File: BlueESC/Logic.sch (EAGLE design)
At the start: 33 parts, among them U1 ATMEGA168, U2 V_REG_LDOSMD, Y1 RESONATORSMD

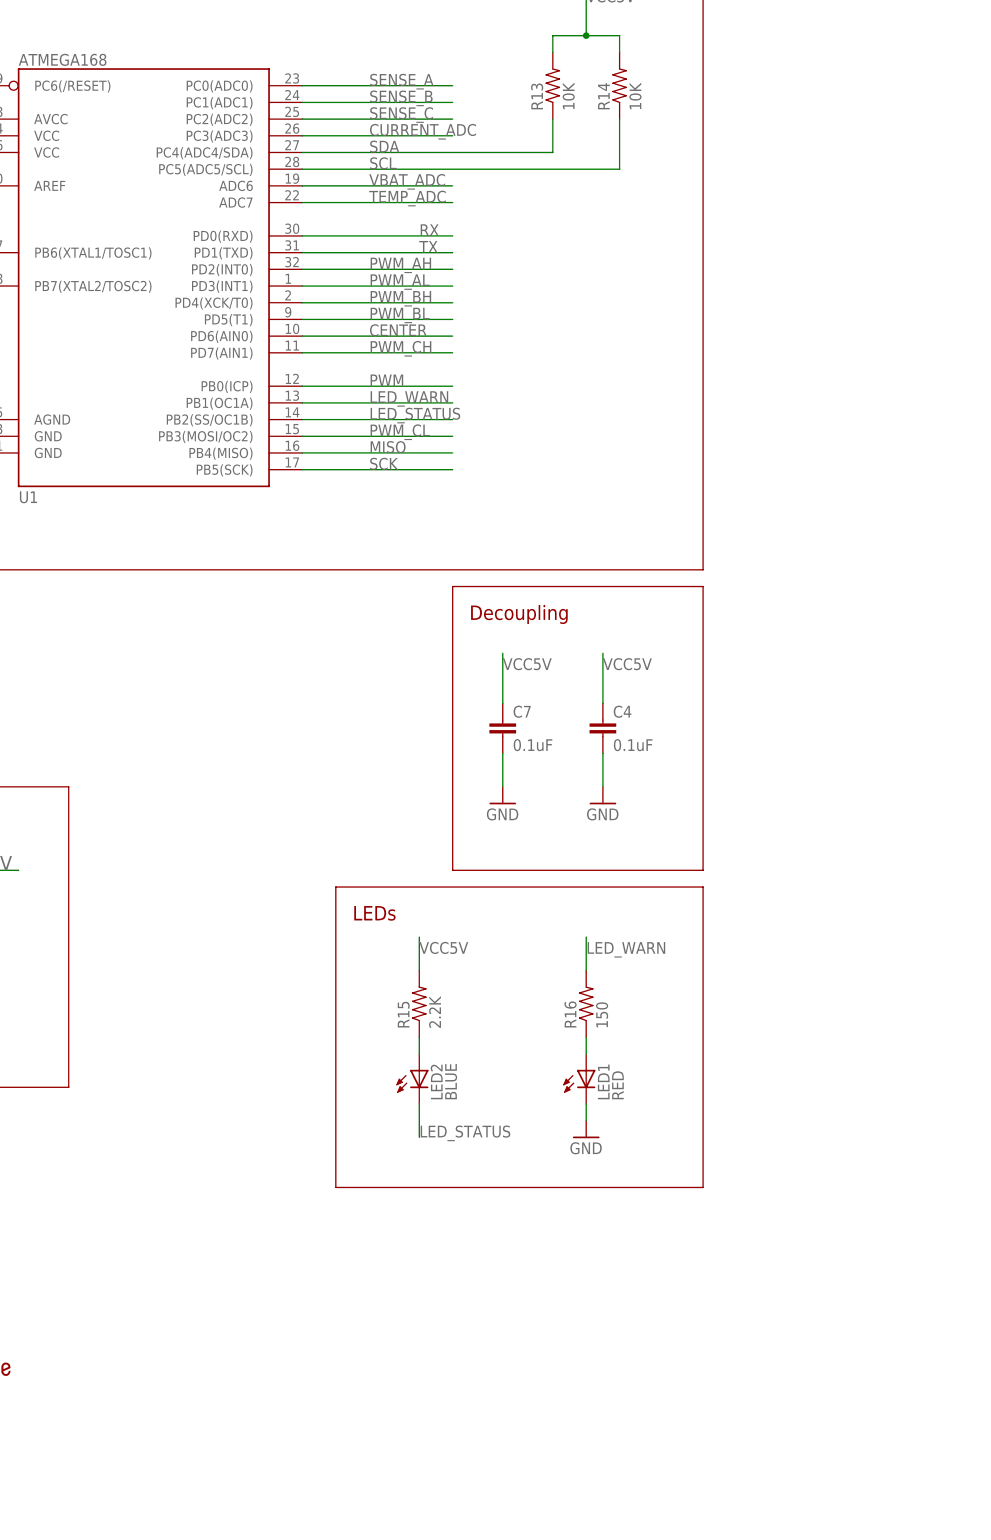
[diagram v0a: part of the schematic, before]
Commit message: Switch to SMT LEDs.
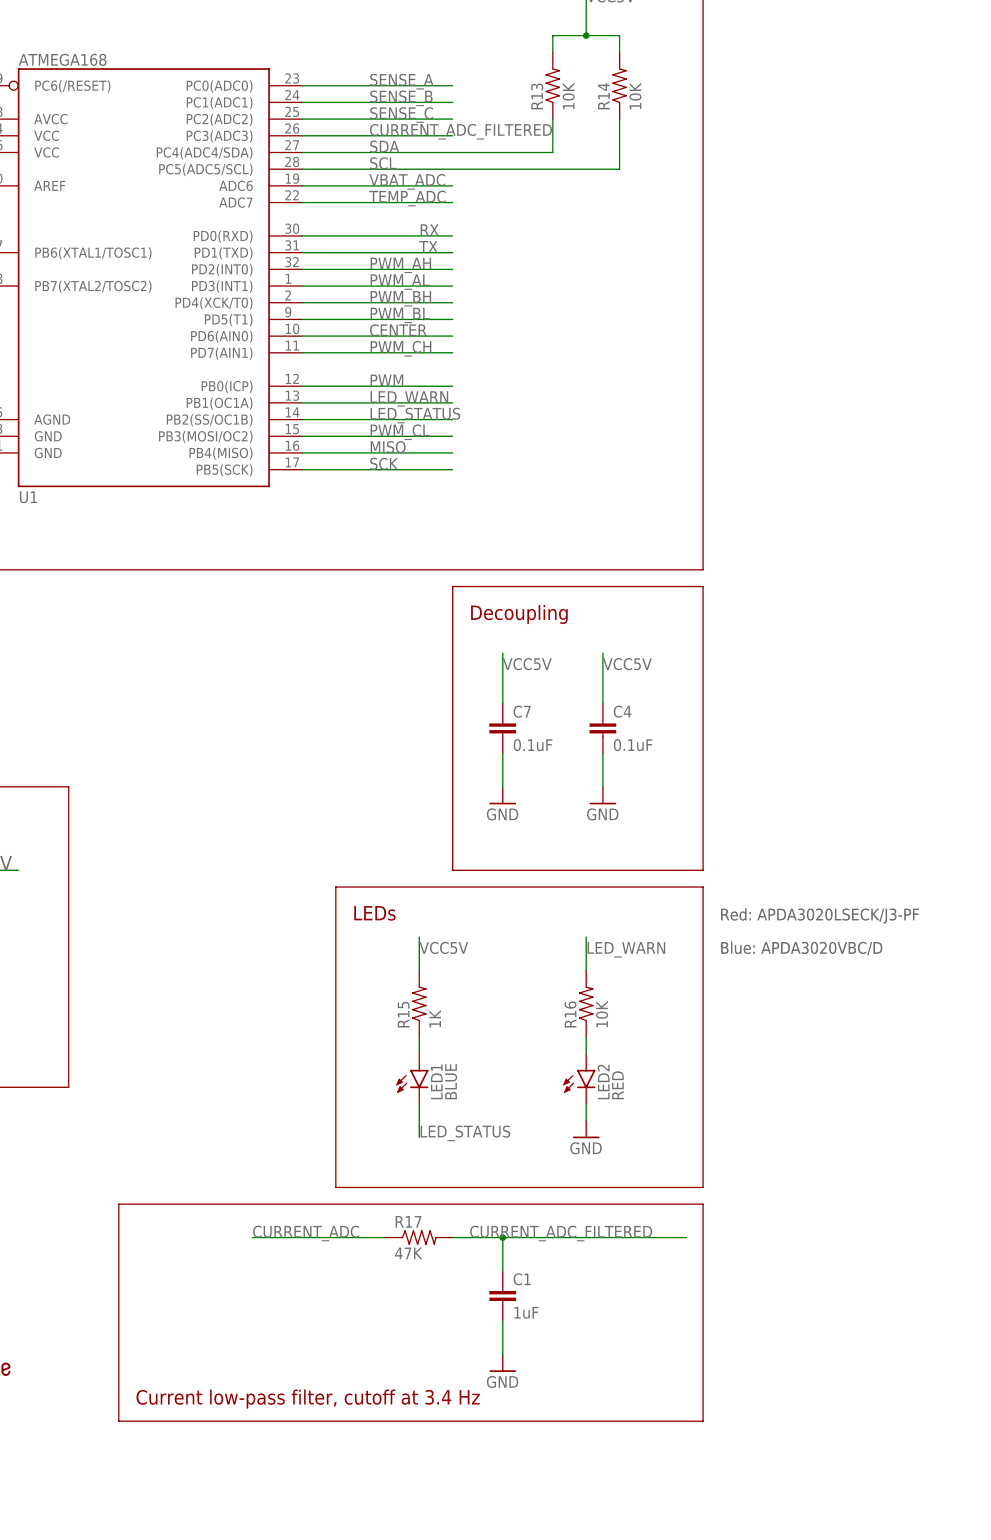
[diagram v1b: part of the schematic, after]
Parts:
- added C1: 1uF, SparkFun-Capacitors:CAP0603-CAP
- added R17: 47K, SparkFun:RESISTOR0603-RES
- LED1: value RED -> BLUE; device SparkFun:LED3MM -> BR-Eagle-Library:LED3X2-RA
- LED2: value BLUE -> RED; device SparkFun:LED3MM -> BR-Eagle-Library:LED3X2-RA
- R15: value 2.2K -> 1K
- R16: value 150 -> 10K
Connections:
- new net CURRENT_ADC_FILTERED: C1.1, R17.2, U1.PC3(ADC3)
- net CURRENT_ADC: now also R17.1; no longer U1.PC3(ADC3)
- net GND: now also C1.2, LED2.C; no longer LED1.C
- net LED_STATUS: now also LED1.C; no longer LED2.C
- net N$16: now also LED1.A; no longer LED2.A
- net N$3: now also LED2.A; no longer LED1.A
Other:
- note added: "Blue: APDA3020VBC/D"
- note added: "Current low-pass filter, cutoff at 3.4 Hz"
- note added: "Red: APDA3020LSECK/J3-PF"

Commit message: Added PWM pull-down resistor.
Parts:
- added R18: 10K, SparkFun:RESISTOR0603-RES
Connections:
- net GND: now also R18.1
- net PWM: now also R18.2
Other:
- note added: "PWM Pull-Down"
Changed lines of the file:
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@@
 <part name="LED1" library="BR-Eagle-Library" deviceset="LED" device="3X2-RA" value="BLUE"/>
 <part name="LED2" library="BR-Eagle-Library" deviceset="LED" device="3X2-RA" value="RED"/>
+<part name="R18" library="SparkFun" deviceset="RESISTOR" device="0603-RES" value="10K"/>
+<part name="GND6" library="SparkFun" deviceset="GND" device=""/>
 </parts>
 <sheets>
@@
 <text x="208.28" y="35.56" size="1.778" layer="97">Red: APDA3020LSECK/J3-PF</text>
 <text x="208.28" y="30.48" size="1.778" layer="97">Blue: APDA3020VBC/D</text>
+<text x="119.38" y="81.28" size="2.1844" layer="94" ratio="13">PWM Pull-Down</text>
 </plain>
 <instances>
@@
 <instance part="LED1" gate="G$1" x="162.56" y="12.7"/>
 <instance part="LED2" gate="G$1" x="187.96" y="12.7"/>
+<instance part="R18" gate="G$1" x="147.32" y="68.58" rot="R90"/>
+<instance part="GND6" gate="1" x="147.32" y="53.34"/>
 </instances>
 <busses>
@@
 <pinref part="C1" gate="G$1" pin="2"/>
 <wire x1="175.26" y1="-30.48" x2="175.26" y2="-25.4" width="0.1524" layer="91"/>
+</segment>
+<segment>
+<pinref part="GND6" gate="1" pin="GND"/>
+<pinref part="R18" gate="G$1" pin="1"/>
+<wire x1="147.32" y1="55.88" x2="147.32" y2="63.5" width="0.1524" layer="91"/>
 </segment>
 </net>
@@
 <label x="-5.08" y="-10.16" size="1.778" layer="95"/>
 </segment>
-</net>
+<segment>
+<pinref part="R18" gate="G$1" pin="2"/>
+<wire x1="147.32" y1="73.66" x2="147.32" y2="83.82" width="0.1524" layer="91"/>
+<label x="147.32" y="81.28" size="1.778" layer="95"/>
+</segment>
+</net>

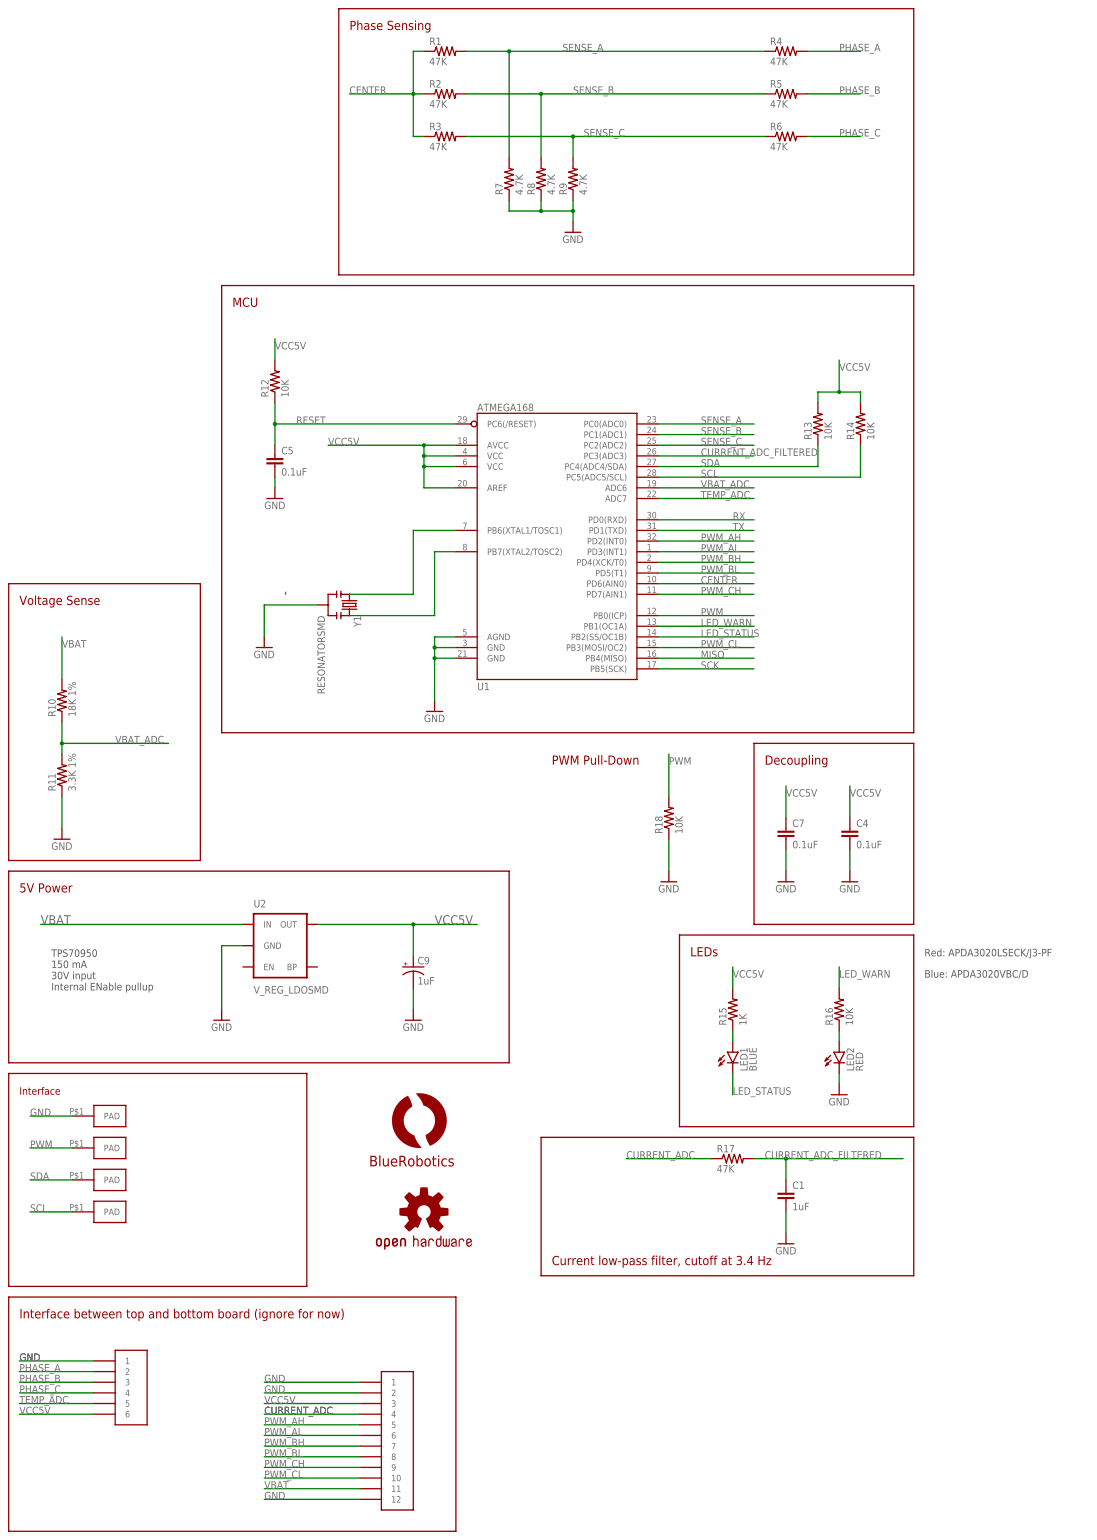
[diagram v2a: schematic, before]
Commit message: New logic board prototype ordered 8/14/15.
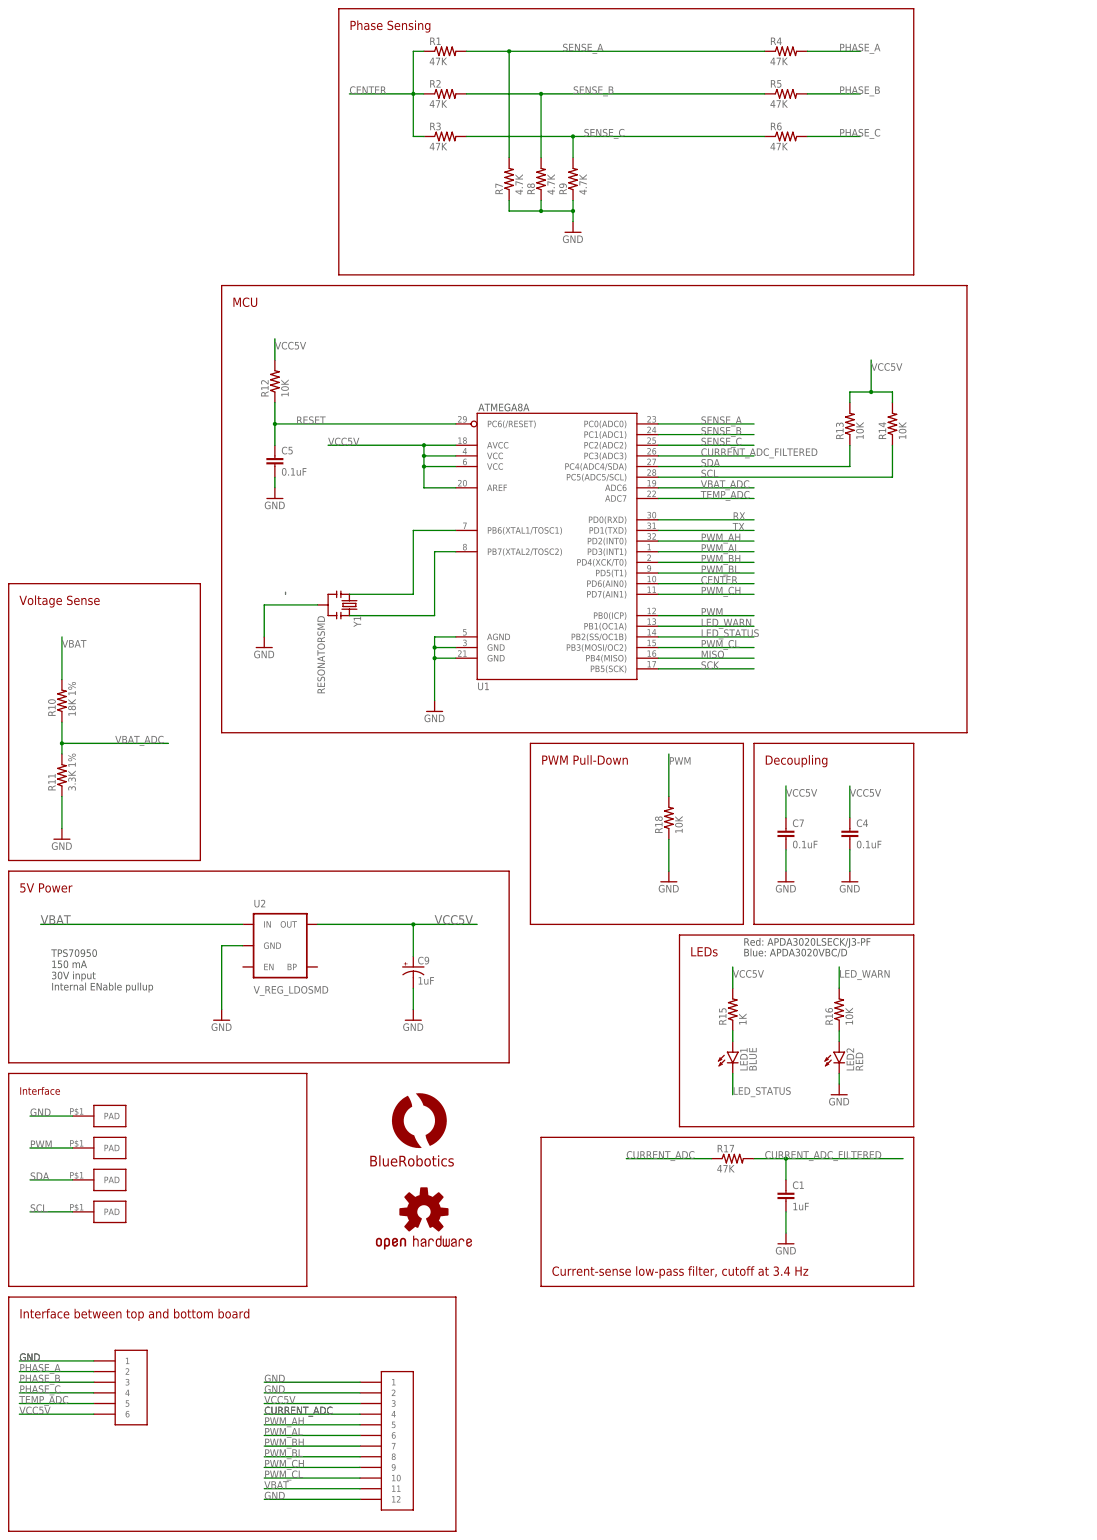
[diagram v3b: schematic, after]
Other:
- note added: "ATMEGA8A"
- note added: "Current-sense low-pass filter, cutoff at 3.4 Hz"
- note added: "Interface between top and bottom board"
- note removed: "Current low-pass filter, cutoff at 3.4 Hz"
- note removed: "Interface between top and bottom board (ignore for now)"
- moved on the sheet: R13, R14
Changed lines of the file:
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@@
 <plain>
 <wire x1="55.88" y1="122.428" x2="55.88" y2="121.92" width="0.2032" layer="97"/>
-<wire x1="40.64" y1="195.58" x2="205.74" y2="195.58" width="0.1524" layer="94"/>
-<wire x1="205.74" y1="195.58" x2="205.74" y2="88.9" width="0.1524" layer="94"/>
-<wire x1="205.74" y1="88.9" x2="40.64" y2="88.9" width="0.1524" layer="94"/>
+<wire x1="40.64" y1="195.58" x2="218.44" y2="195.58" width="0.1524" layer="94"/>
+<wire x1="218.44" y1="195.58" x2="218.44" y2="88.9" width="0.1524" layer="94"/>
+<wire x1="218.44" y1="88.9" x2="40.64" y2="88.9" width="0.1524" layer="94"/>
 <wire x1="40.64" y1="88.9" x2="40.64" y2="195.58" width="0.1524" layer="94"/>
 <text x="43.18" y="190.5" size="2.1844" layer="94" ratio="13">MCU</text>
@@
 <wire x1="96.52" y1="-101.6" x2="-10.16" y2="-101.6" width="0.1524" layer="94"/>
 <wire x1="-10.16" y1="-101.6" x2="-10.16" y2="-45.72" width="0.1524" layer="94"/>
-<text x="-7.62" y="-50.8" size="2.1844" layer="94" ratio="13">Interface between top and bottom board (ignore for now)</text>
+<text x="-7.62" y="-50.8" size="2.1844" layer="94" ratio="13">Interface between top and bottom board</text>
 <wire x1="205.74" y1="-7.62" x2="116.84" y2="-7.62" width="0.1524" layer="94"/>
-<wire x1="116.84" y1="-7.62" x2="116.84" y2="-40.64" width="0.1524" layer="94"/>
-<wire x1="116.84" y1="-40.64" x2="205.74" y2="-40.64" width="0.1524" layer="94"/>
-<wire x1="205.74" y1="-40.64" x2="205.74" y2="-7.62" width="0.1524" layer="94"/>
-<text x="119.38" y="-38.1" size="2.1844" layer="94" ratio="13">Current low-pass filter, cutoff at 3.4 Hz</text>
-<text x="208.28" y="35.56" size="1.778" layer="97">Red: APDA3020LSECK/J3-PF</text>
-<text x="208.28" y="30.48" size="1.778" layer="97">Blue: APDA3020VBC/D</text>
-<text x="119.38" y="81.28" size="2.1844" layer="94" ratio="13">PWM Pull-Down</text>
+<wire x1="116.84" y1="-7.62" x2="116.84" y2="-43.18" width="0.1524" layer="94"/>
+<wire x1="116.84" y1="-43.18" x2="205.74" y2="-43.18" width="0.1524" layer="94"/>
+<wire x1="205.74" y1="-43.18" x2="205.74" y2="-7.62" width="0.1524" layer="94"/>
+<text x="119.38" y="-40.64" size="2.1844" layer="94" ratio="13">Current-sense low-pass filter, cutoff at 3.4 Hz</text>
+<text x="165.1" y="38.1" size="1.778" layer="97">Red: APDA3020LSECK/J3-PF</text>
+<text x="165.1" y="35.56" size="1.778" layer="97">Blue: APDA3020VBC/D</text>
+<text x="116.84" y="81.28" size="2.1844" layer="94" ratio="13">PWM Pull-Down</text>
+<text x="101.854" y="165.608" size="1.778" layer="97">ATMEGA8A</text>
+<wire x1="114.3" y1="86.36" x2="165.1" y2="86.36" width="0.1524" layer="94"/>
+<wire x1="165.1" y1="86.36" x2="165.1" y2="43.18" width="0.1524" layer="94"/>
+<wire x1="165.1" y1="43.18" x2="114.3" y2="43.18" width="0.1524" layer="94"/>
+<wire x1="114.3" y1="43.18" x2="114.3" y2="86.36" width="0.1524" layer="94"/>
 </plain>
 <instances>
-<instance part="U1" gate="G$1" x="119.38" y="137.16"/>
+<instance part="U1" gate="G$1" x="119.38" y="137.16" smashed="yes">
+<attribute name="NAME" x="101.6" y="99.06" size="1.778" layer="95"/>
+</instance>
 <instance part="R1" gate="G$1" x="93.98" y="251.46"/>
 <instance part="R2" gate="G$1" x="93.98" y="241.3"/>
@@
 <instance part="GND4" gate="1" x="53.34" y="144.78"/>
 <instance part="GND5" gate="1" x="91.44" y="93.98"/>
-<instance part="R13" gate="G$1" x="182.88" y="162.56" rot="R90"/>
-<instance part="R14" gate="G$1" x="193.04" y="162.56" rot="R90"/>
+<instance part="R13" gate="G$1" x="190.5" y="162.56" rot="R90"/>
+<instance part="R14" gate="G$1" x="200.66" y="162.56" rot="R90"/>
 <instance part="GND9" gate="1" x="50.8" y="109.22"/>
 <instance part="Y1" gate="G$1" x="71.12" y="119.38" rot="R270"/>
@@
 <segment>
 <pinref part="R13" gate="G$1" pin="2"/>
-<wire x1="182.88" y1="167.64" x2="182.88" y2="170.18" width="0.1524" layer="91"/>
+<wire x1="190.5" y1="167.64" x2="190.5" y2="170.18" width="0.1524" layer="91"/>
 <pinref part="R14" gate="G$1" pin="2"/>
-<wire x1="182.88" y1="170.18" x2="187.96" y2="170.18" width="0.1524" layer="91"/>
-<wire x1="187.96" y1="170.18" x2="193.04" y2="170.18" width="0.1524" layer="91"/>
-<wire x1="193.04" y1="170.18" x2="193.04" y2="167.64" width="0.1524" layer="91"/>
-<wire x1="187.96" y1="170.18" x2="187.96" y2="177.8" width="0.1524" layer="91"/>
-<junction x="187.96" y="170.18"/>
-<label x="187.96" y="175.26" size="1.778" layer="95"/>
+<wire x1="190.5" y1="170.18" x2="195.58" y2="170.18" width="0.1524" layer="91"/>
+<wire x1="195.58" y1="170.18" x2="200.66" y2="170.18" width="0.1524" layer="91"/>
+<wire x1="200.66" y1="170.18" x2="200.66" y2="167.64" width="0.1524" layer="91"/>
+<wire x1="195.58" y1="170.18" x2="195.58" y2="177.8" width="0.1524" layer="91"/>
+<junction x="195.58" y="170.18"/>
+<label x="195.58" y="175.26" size="1.778" layer="95"/>
 </segment>
 <segment>
@@
 <segment>
 <pinref part="U1" gate="G$1" pin="PC4(ADC4/SDA)"/>
-<wire x1="144.78" y1="152.4" x2="182.88" y2="152.4" width="0.1524" layer="91"/>
+<wire x1="144.78" y1="152.4" x2="190.5" y2="152.4" width="0.1524" layer="91"/>
 <label x="154.94" y="152.4" size="1.778" layer="95"/>
 <pinref part="R13" gate="G$1" pin="1"/>
-<wire x1="182.88" y1="152.4" x2="182.88" y2="157.48" width="0.1524" layer="91"/>
+<wire x1="190.5" y1="152.4" x2="190.5" y2="157.48" width="0.1524" layer="91"/>
 </segment>
 <segment>
@@
 <label x="154.94" y="149.86" size="1.778" layer="95"/>
 <pinref part="R14" gate="G$1" pin="1"/>
-<wire x1="144.78" y1="149.86" x2="193.04" y2="149.86" width="0.1524" layer="91"/>
-<wire x1="193.04" y1="149.86" x2="193.04" y2="157.48" width="0.1524" layer="91"/>
-</segment>
-<segment>
+<wire x1="144.78" y1="149.86" x2="200.66" y2="149.86" width="0.1524" layer="91"/>
+<wire x1="200.66" y1="149.86" x2="200.66" y2="157.48" width="0.1524" layer="91"/>
+</segment>
+<segment>
